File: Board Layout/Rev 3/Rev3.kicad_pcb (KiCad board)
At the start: 2 copper layers, 22.9 x 14 mm, 7 parts, among them P1 CONN_01X05, P2 CONN_01X05

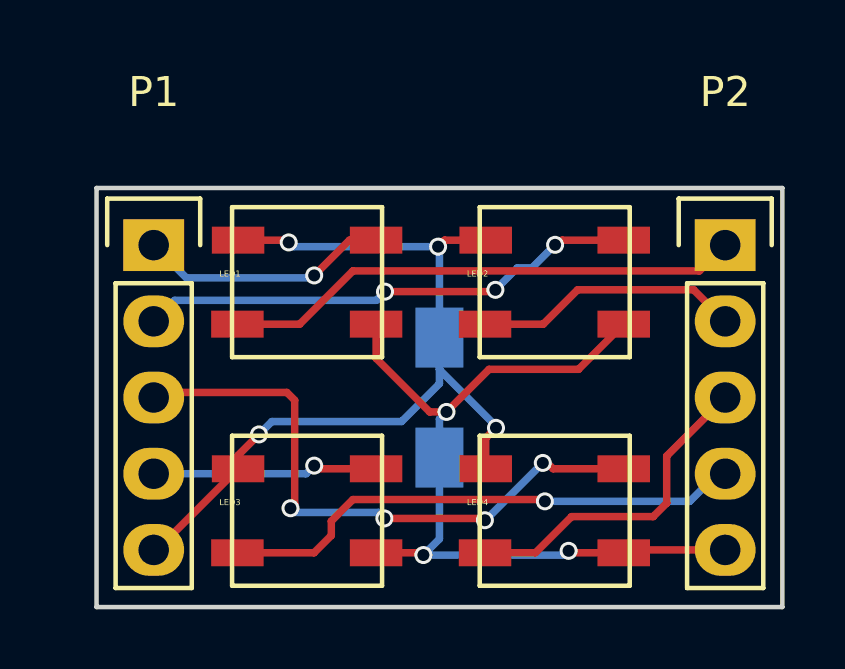
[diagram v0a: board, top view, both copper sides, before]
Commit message: Rev 3 - 2
Added Silk Screen for Pin/LED numbers. Corrected gerbers, sent off the
zip file to oshpark./
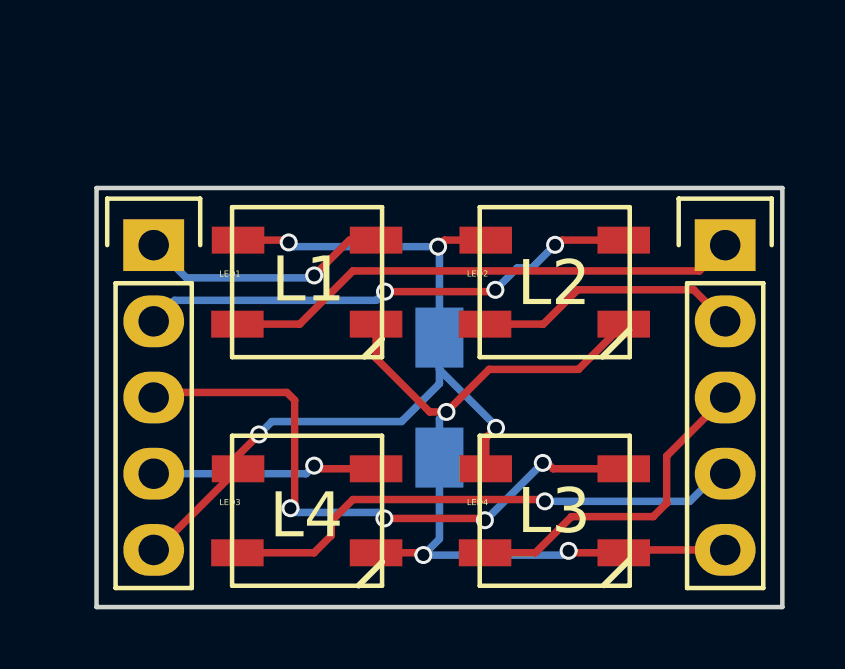
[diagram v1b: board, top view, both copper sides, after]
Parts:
- renumbered P1 to ?, P2 to ?
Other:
- board text added: "5V"
- board text added: "DI1"
- board text added: "DI2"
- board text added: "DI3"
- board text added: "DI4"
- board text added: "DO1"
- board text added: "DO2"
- board text added: "DO3"
- board text added: "DO4"
- board text added: "GND"
- board text added: "L1"
- board text added: "L2"
- board text added: "L3"
- board text added: "L4"

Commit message: New Update
Created a new layout. More condensed. Uses 4 Caps.
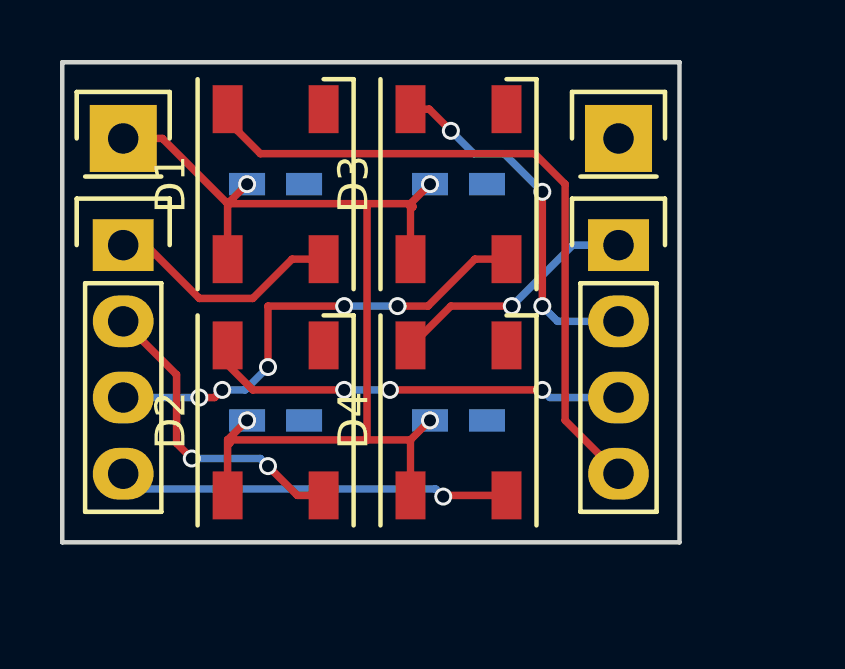
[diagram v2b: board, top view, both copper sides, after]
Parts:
- removed ? (x2): CONN_01X05, Pin_Headers:Pin_Header_Straight_1x05
- removed LED1, LED2, LED3, LED4: WS2812, Rev 3:WS2812B
- added C2: C_Small, Capacitors_SMD:C_0603_HandSoldering, B.Cu at (142.5, 108.7)
- added C3: C_Small, Capacitors_SMD:C_0603_HandSoldering, B.Cu at (148.6, 100.8)
- added C4: C_Small, Capacitors_SMD:C_0603_HandSoldering, B.Cu at (148.6, 108.7)
- added D1: WS2812B, LEDs:LED_WS2812B-PLCC4, F.Cu at (142.5, 100.8)
- added D2: WS2812B, LEDs:LED_WS2812B-PLCC4, F.Cu at (142.5, 108.7)
- added D3: WS2812B, LEDs:LED_WS2812B-PLCC4, F.Cu at (148.6, 100.8)
- added D4: WS2812B, LEDs:LED_WS2812B-PLCC4, F.Cu at (148.6, 108.7)
- added DIN: DIN, Pin_Headers:Pin_Header_Straight_1x04, F.Cu at (153.9, 102.9)
- added Dout: DOUT, Pin_Headers:Pin_Header_Straight_1x04, F.Cu at (137.4, 102.9)
- added VDD: VDD, Pin_Headers:Pin_Header_Straight_1x01, F.Cu at (137.4, 99.3)
- added VSS: VSS, Pin_Headers:Pin_Header_Straight_1x01, F.Cu at (153.9, 99.3)
- C1: value C -> C_Small; footprint Capacitors_SMD:C_1206_HandSoldering -> Capacitors_SMD:C_0603_HandSoldering
- moved C1 8.97 mm to (142.5, 100.8), turned to 0 degrees
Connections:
- C1 pad 1: Net-(C1-Pad1) -> +5V
- C1 pad 2: Net-(C1-Pad2) -> GND
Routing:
- net +5V: track 0.00 -> 36.6 mm, vias 0 -> 4
- net Net-(C1-Pad2): track 31.2 -> 0.00 mm, vias 4 -> 0
- net Net-(C1-Pad1): track 28.6 -> 0.00 mm, vias 3 -> 0
- net Net-(D1-Pad4): track 0.00 -> 22.9 mm
- net Net-(LED4-Pad2): track 20.7 -> 0.00 mm, vias 4 -> 0
- net Net-(LED3-Pad4): track 17.7 -> 0.00 mm, vias 1 -> 0
- net Net-(LED1-Pad4): track 17.4 -> 0.00 mm
- net Net-(LED2-Pad2): track 16.8 -> 0.00 mm, vias 3 -> 0
- net Net-(D3-Pad2): track 0.00 -> 16.1 mm, vias 0 -> 5
- net Net-(D2-Pad4): track 0.00 -> 14.1 mm, vias 0 -> 3
- net Net-(D4-Pad2): track 0.00 -> 13.6 mm, vias 0 -> 1
- net Net-(D3-Pad4): track 0.00 -> 12.1 mm, vias 0 -> 3
- net Net-(LED4-Pad4): track 11.1 -> 0.00 mm
- net Net-(D2-Pad2): track 0.00 -> 10.7 mm, vias 0 -> 2
- net Net-(LED2-Pad4): track 8.91 -> 0.00 mm
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- added copper zone on B.Cu, net GND
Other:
- board size 22.9 x 14 mm -> 20.6 x 16 mm
- board text added: "1"
- board text removed: "5V"
- board text removed: "DI1"
- board text removed: "DI2"
- board text removed: "DI3"
- board text removed: "DI4"
- board text removed: "DO1"
- board text removed: "DO2"
- board text removed: "DO3"
- board text removed: "DO4"
- board text removed: "GND"
- board text removed: "L1"
- board text removed: "L2"
- board text removed: "L3"
- board text removed: "L4"

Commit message: Sent
Fixed and sent fof an order off 500 of this revision.
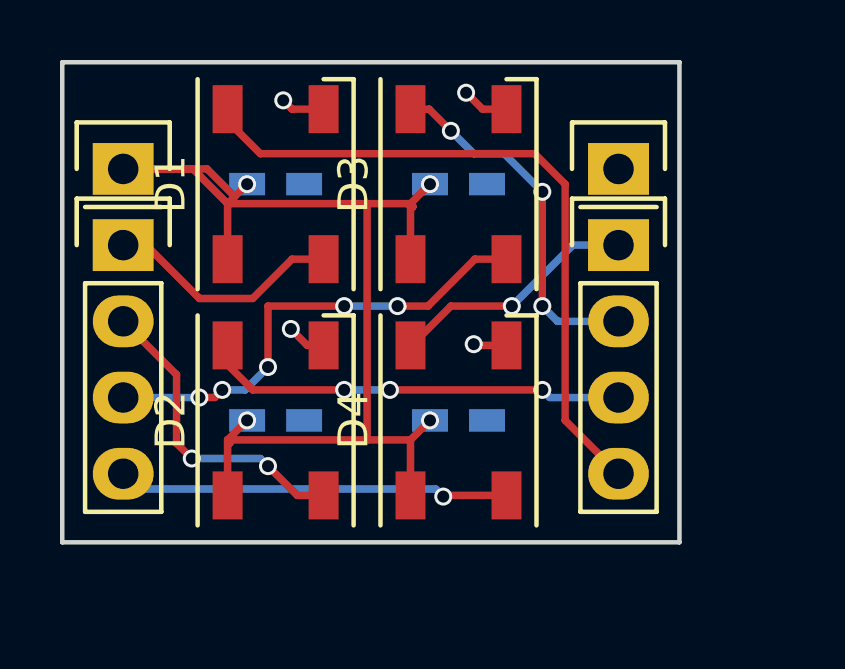
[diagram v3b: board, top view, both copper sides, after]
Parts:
- moved VDD 1.02 mm to (137.4, 100.3)
- moved VSS 1.02 mm to (153.9, 100.3)
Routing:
- net GND: track 0.00 -> 5.47 mm, vias 0 -> 4
- net +5V: track 36.6 -> 39.9 mm
